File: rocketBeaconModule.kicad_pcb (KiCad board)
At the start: 2 copper layers, 46.2 x 46.3 mm, 74 parts, among them J1 TYPE-C-31-M-12, P1 AntMount, U1 STM32F401CCU6, U2 CP2102N-Axx-xQFN20, U3 CC1200, X1 40MHz, Y1 16MHz

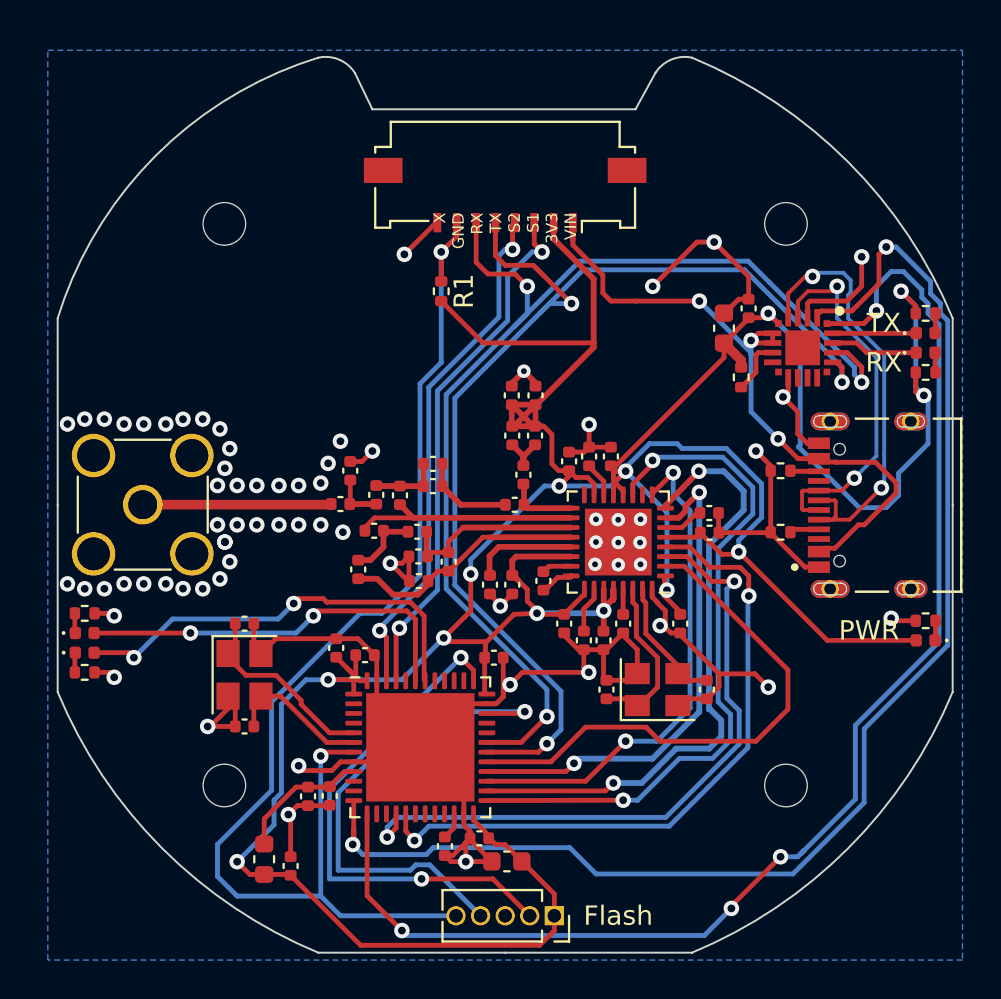
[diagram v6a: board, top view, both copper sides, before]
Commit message: added power pads
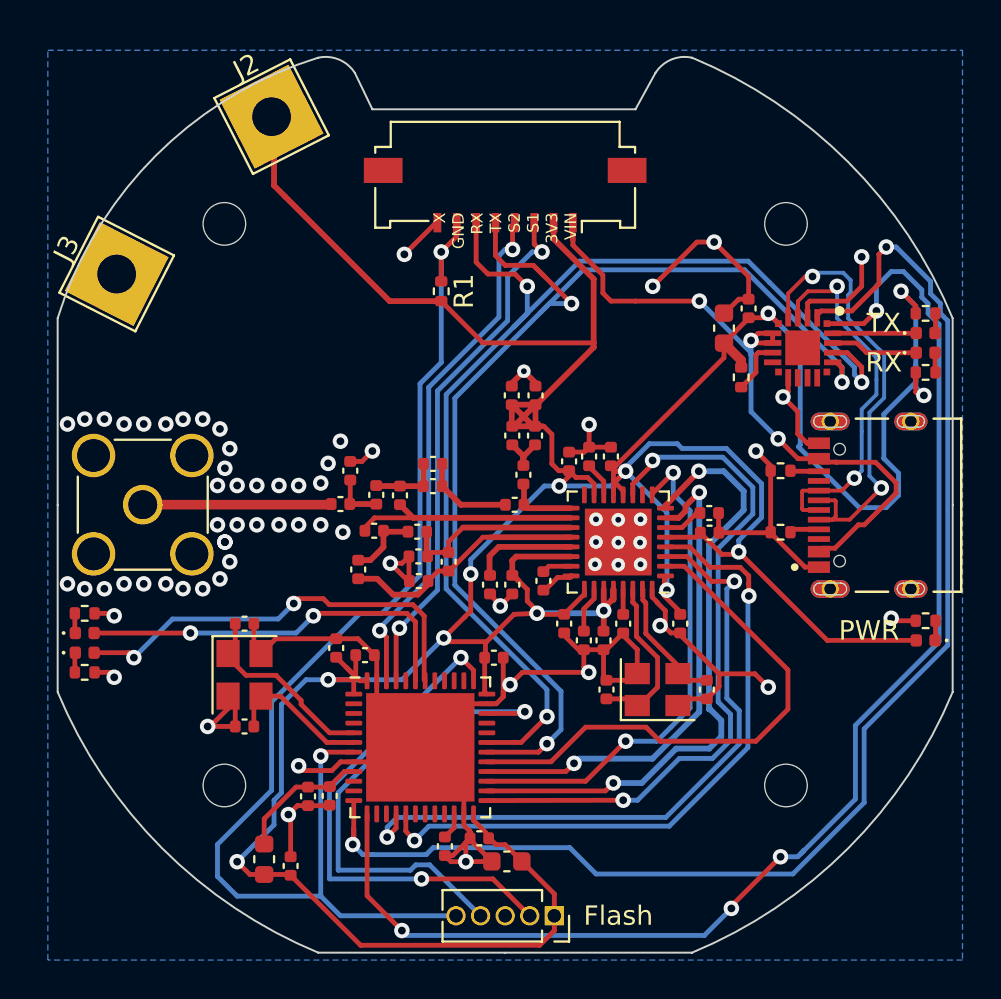
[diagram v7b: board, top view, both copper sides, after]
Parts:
- added J2: PWR, TestPoint:TestPoint_THTPad_4.0x4.0mm_Drill2.0mm, F.Cu at (59.9, 106.7)
- added J3: GND, TestPoint:TestPoint_THTPad_4.0x4.0mm_Drill2.0mm, F.Cu at (51.9, 114.8)
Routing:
- net +3.3V: track 212.1 -> 228.5 mm
- net /D-: track 23.2 -> 24.1 mm

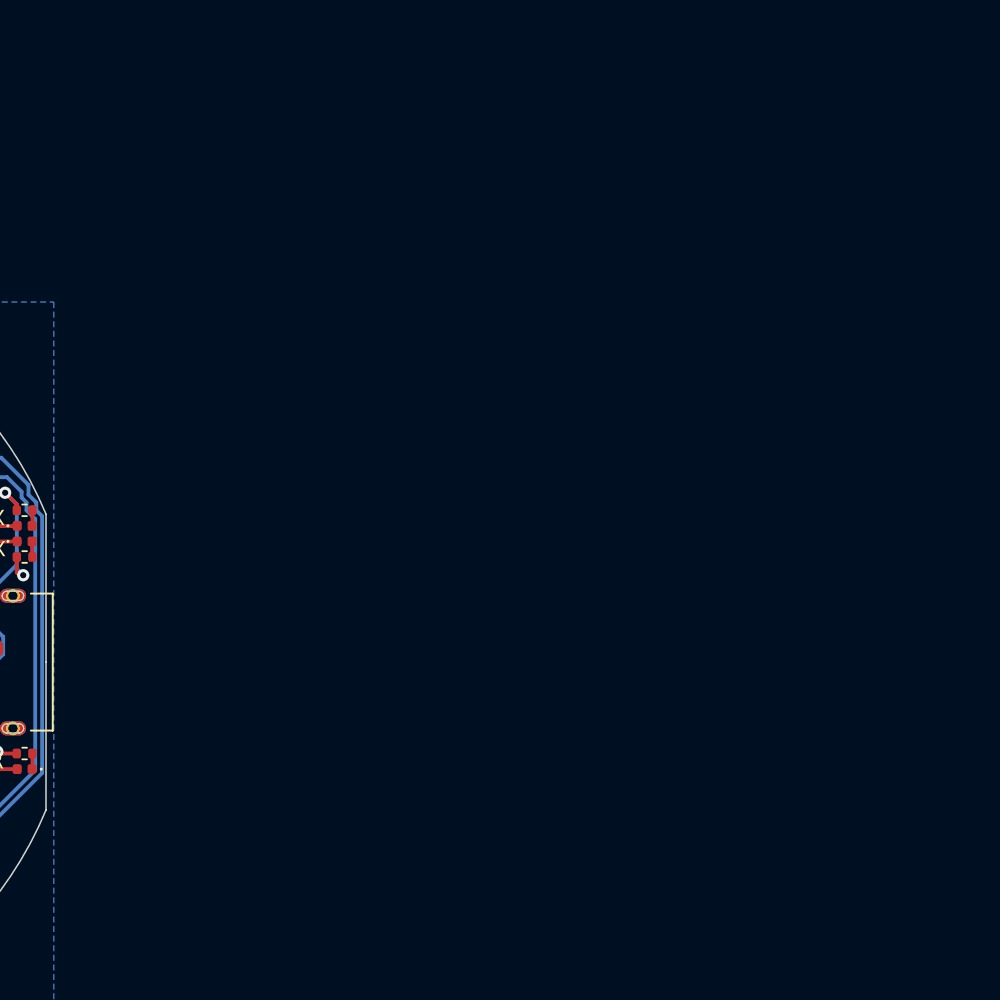
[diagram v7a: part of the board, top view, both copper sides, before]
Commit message: Added larger 60mm cutout to match rocket club *note this is not nescesary since mounting holes line up between both sizes, it would be purely aesthetic
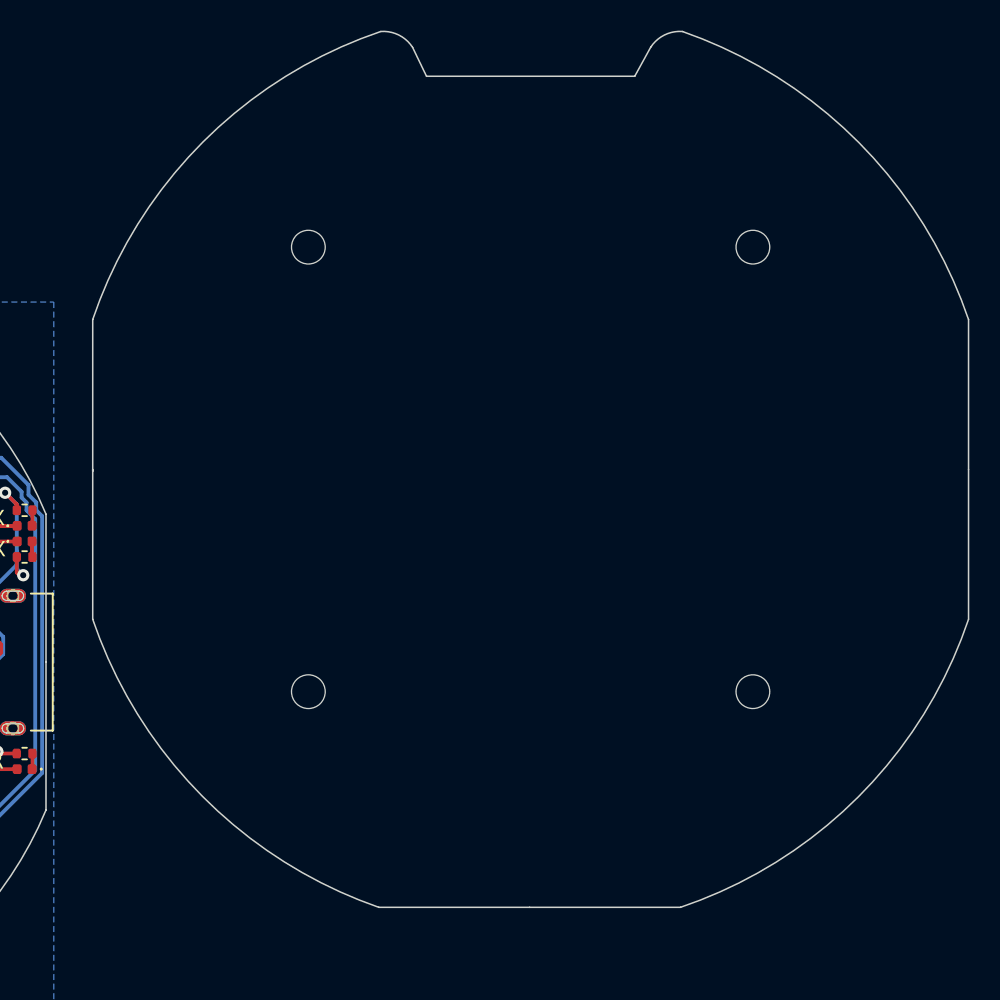
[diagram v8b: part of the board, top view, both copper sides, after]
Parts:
- added ?: , , F.Cu at (141.2, 128.7)
- added ?: , , F.Cu at (112.2, 128.7)
- added ?: , , F.Cu at (141.2, 99.7)
- added ?: , , F.Cu at (112.2, 99.7)
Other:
- board size 46.2 x 46.3 mm -> 106.4 x 64.3 mm
- board text added: "CIRCLE CENTER"
- board text added: "CIRCLE EDGE"
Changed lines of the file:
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@@
     )
   )
+  (footprint "" (layer "F.Cu")
+    (at 141.2494 128.6764)
+    (fp_text reference "" (at 0 0) (layer "F.SilkS")
+      (effects (font (size 1.27 1.27) (thickness 0.15)))
+    )
+    (fp_text value "" (at 0 0) (layer "F.SilkS")
+      (effects (font (size 1.27 1.27) (thickness 0.15)))
+    )
+    (pad "" np_thru_hole circle (at 0 0) (size 2.2 2.2) (drill 2.2) (layers *.Cu *.Mask))
+  )
   (footprint "CP2102:WFQFN-20" (layer "F.Cu")
     (at 87.376 118.618 -90)
@@
     (pad "" np_thru_hole circle (at 0 0) (size 2.2 2.2) (drill 2.2) (layers *.Cu *.Mask))
   )
+  (footprint "" (layer "F.Cu")
+    (at 112.2426 128.6764)
+    (fp_text reference "" (at 0 0) (layer "F.SilkS")
+      (effects (font (size 1.27 1.27) (thickness 0.15)))
+    )
+    (fp_text value "" (at 0 0) (layer "F.SilkS")
+      (effects (font (size 1.27 1.27) (thickness 0.15)))
+    )
+    (pad "" np_thru_hole circle (at 0 0) (size 2.2 2.2) (drill 2.2) (layers *.Cu *.Mask))
+  )
   (footprint "Capacitor_SMD:C_0402_1005Metric" (layer "F.Cu")
     (at 65.351 126.213 -90)
@@
     )
   )
+  (footprint "" (layer "F.Cu")
+    (at 141.2494 99.6696)
+    (fp_text reference "" (at 0 0) (layer "F.SilkS")
+      (effects (font (size 1.27 1.27) (thickness 0.15)))
+    )
+    (fp_text value "" (at 0 0) (layer "F.SilkS")
+      (effects (font (size 1.27 1.27) (thickness 0.15)))
+    )
+    (pad "" np_thru_hole circle (at 0 0) (size 2.2 2.2) (drill 2.2) (layers *.Cu *.Mask))
+  )
   (footprint "Capacitor_SMD:C_0402_1005Metric" (layer "F.Cu")
     (at 67.469 128.117)
@@
     )
   )
+  (footprint "" (layer "F.Cu")
+    (at 112.2426 99.6696)
+    (fp_text reference "" (at 0 0) (layer "F.SilkS")
+      (effects (font (size 1.27 1.27) (thickness 0.15)))
+    )
+    (fp_text value "" (at 0 0) (layer "F.SilkS")
+      (effects (font (size 1.27 1.27) (thickness 0.15)))
+    )
+    (pad "" np_thru_hole circle (at 0 0) (size 2.2 2.2) (drill 2.2) (layers *.Cu *.Mask))
+  )
   (footprint "Capacitor_SMD:C_0402_1005Metric" (layer "F.Cu")
     (at 64.419 130.067 90)
@@
     )
   )
+  (gr_line (start 126.619 114.3) (end 126.746 114.173) (layer "Cmts.User") (width 0.15))
+  (gr_line (start 156.972 114.173) (end 157.099 114.3) (layer "Cmts.User") (width 0.15))
+  (gr_line (start 126.746 114.173) (end 126.873 114.046) (layer "Cmts.User") (width 0.15))
+  (gr_line (start 156.972 114.173) (end 157.099 114.046) (layer "Cmts.User") (width 0.15))
+  (gr_line (start 156.972 114.173) (end 126.746 114.173) (layer "Cmts.User") (width 0.15))
+  (gr_line (start 126.746 114.173) (end 126.873 114.3) (layer "Cmts.User") (width 0.15))
+  (gr_line (start 156.845 114.3) (end 156.972 114.173) (layer "Cmts.User") (width 0.15))
+  (gr_line (start 126.619 114.046) (end 126.746 114.173) (layer "Cmts.User") (width 0.15))
+  (gr_line (start 156.845 114.046) (end 156.972 114.173) (layer "Cmts.User") (width 0.15))
+  (gr_line (start 126.873 114.046) (end 126.746 114.173) (layer "Cmts.User") (width 0.15))
+  (gr_line (start 157.099 114.046) (end 156.972 114.173) (layer "Cmts.User") (width 0.15))
   (gr_line (start 62.357 149.86) (end 72.009 149.86) (layer "Edge.Cuts") (width 0.1))
+  (gr_line (start 119.043354 86.633146) (end 119.9515 88.519) (layer "Edge.Cuts") (width 0.1))
   (gr_line (start 48.895 117.094) (end 48.895 126.746) (layer "Edge.Cuts") (width 0.1))
   (gr_arc (start 81.661 103.632) (mid 89.72889 109.02611) (end 95.123 117.094) (layer "Edge.Cuts") (width 0.1))
+  (gr_arc (start 155.321 123.952) (mid 148.121691 135.548691) (end 136.525 142.748) (layer "Edge.Cuts") (width 0.1))
+  (gr_arc (start 136.652 85.598) (mid 148.158246 92.838927) (end 155.321 104.394) (layer "Edge.Cuts") (width 0.1))
+  (gr_line (start 126.682501 142.748001) (end 116.840002 142.748) (layer "Edge.Cuts") (width 0.1))
+  (gr_line (start 98.171 114.3) (end 98.171 104.394) (layer "Edge.Cuts") (width 0.1))
   (gr_arc (start 62.357 103.632) (mid 63.422215 103.727337) (end 64.242854 104.413146) (layer "Edge.Cuts") (width 0.1))
   (gr_arc (start 48.895 117.094) (mid 53.959104 108.696104) (end 62.357 103.632) (layer "Edge.Cuts") (width 0.1))
   (gr_line (start 95.123 136.398) (end 95.123 126.746) (layer "Edge.Cuts") (width 0.1))
   (gr_line (start 64.242854 104.413146) (end 65.151 106.299) (layer "Edge.Cuts") (width 0.1))
+  (gr_arc (start 116.840002 142.748) (mid 105.33333 135.507494) (end 98.171 123.952) (layer "Edge.Cuts") (width 0.1))
   (gr_arc (start 79.775146 104.413146) (mid 80.595774 103.727318) (end 81.661 103.632) (layer "Edge.Cuts") (width 0.1))
+  (gr_arc (start 134.575646 86.633146) (mid 135.471375 85.829844) (end 136.652 85.598) (layer "Edge.Cuts") (width 0.1))
+  (gr_line (start 119.9515 88.519) (end 133.5405 88.519) (layer "Edge.Cuts") (width 0.1))
   (gr_line (start 65.151 106.299) (end 78.74 106.299) (layer "Edge.Cuts") (width 0.1))
   (gr_line (start 72.009 149.86) (end 81.661 149.86) (layer "Edge.Cuts") (width 0.1))
+  (gr_line (start 98.171 123.952) (end 98.171 114.173) (layer "Edge.Cuts") (width 0.1))
   (gr_line (start 48.895 126.746) (end 48.895 136.398) (layer "Edge.Cuts") (width 0.1))
+  (gr_line (start 155.321 114.173) (end 155.321 104.394) (layer "Edge.Cuts") (width 0.1))
+  (gr_line (start 155.321 123.952) (end 155.321 114.173) (layer "Edge.Cuts") (width 0.1))
   (gr_arc (start 62.357 149.86) (mid 54.28911 144.46589) (end 48.895 136.398) (layer "Edge.Cuts") (width 0.1))
   (gr_arc (start 95.123 136.398) (mid 89.72889 144.46589) (end 81.661 149.86) (layer "Edge.Cuts") (width 0.1))
+  (gr_arc (start 98.171 104.394) (mid 105.372789 92.799788) (end 116.967 85.597999) (layer "Edge.Cuts") (width 0.1))
   (gr_line (start 95.123 126.746) (end 95.123 117.094) (layer "Edge.Cuts") (width 0.1))
+  (gr_line (start 136.525 142.748) (end 126.682501 142.748001) (layer "Edge.Cuts") (width 0.1))
   (gr_line (start 79.775146 104.413146) (end 78.74 106.299) (layer "Edge.Cuts") (width 0.1))
+  (gr_arc (start 116.967 85.597999) (mid 118.147622 85.829851) (end 119.043354 86.633146) (layer "Edge.Cuts") (width 0.1))
+  (gr_line (start 134.575646 86.633146) (end 133.5405 88.519) (layer "Edge.Cuts") (width 0.1))
   (gr_text "50mm" (at 62.103 119.126) (layer "B.SilkS")
     (effects (font (size 1 1) (thickness 0.15)) (justify mirror))
@@
     (effects (font (size 1 1) (thickness 0.15)))
   )
+  (gr_text "CIRCLE CENTER" (at 125.984 114.173) (layer "Cmts.User")
+    (effects (font (size 0.1 0.1) (thickness 0.025)))
+  )
+  (gr_text "CIRCLE EDGE\n" (at 157.861 114.173) (layer "Cmts.User")
+    (effects (font (size 0.1 0.1) (thickness 0.025)))
+  )
   (segment (start 64.1885 139.504) (end 62.68 139.504) (width 0.25) (layer "F.Cu") (net 1))
